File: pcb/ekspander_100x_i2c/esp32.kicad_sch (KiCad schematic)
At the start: 32 parts, among them IC1 ESP32-S3-WROOM-1U-N16R8, J25 USB4145-03-0230-C, U13 AP63203WU, U39 USBLC6-2SC6, U41 CP2102N-A02-GQFN20

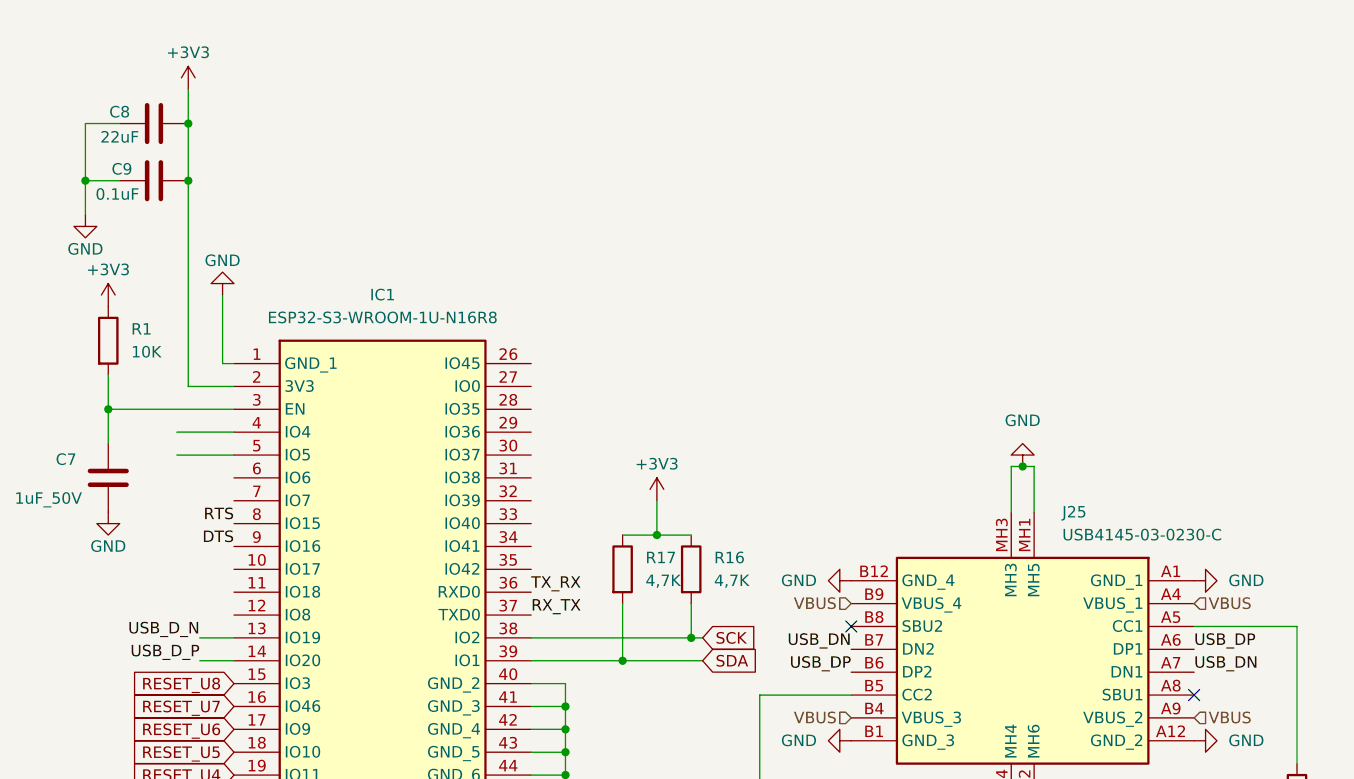
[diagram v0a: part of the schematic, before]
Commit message: Ekspander 100x - RS485
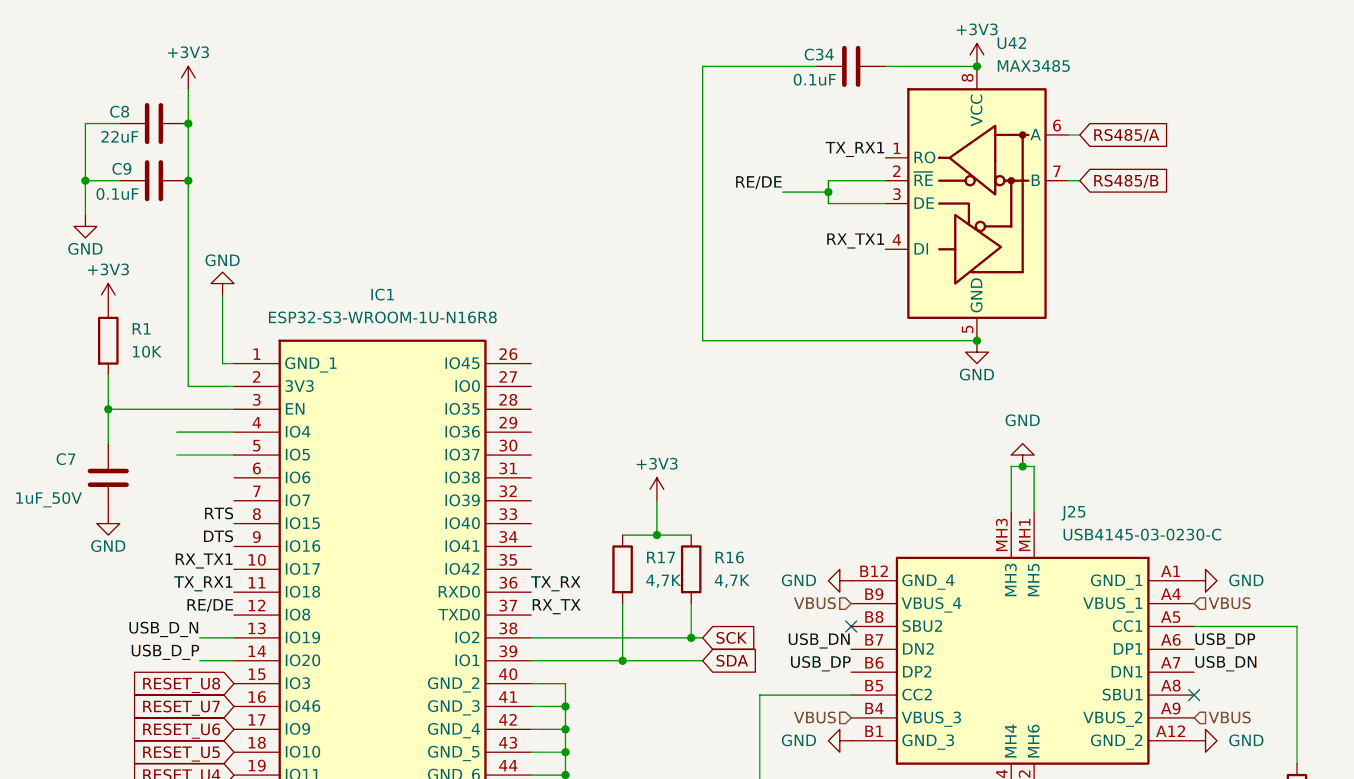
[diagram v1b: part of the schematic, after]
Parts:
- added C34: 0.1uF, Capacitor_SMD:C_0805_2012Metric_Pad1.18x1.45mm_HandSolder, symbol Device:C
- added U42: MAX3485, Package_SO:SOIC-8_3.9x4.9mm_P1.27mm, symbol Interface_UART:MAX3485
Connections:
- net +3V3: now also C34.2, U42.8 (VCC)
- net GND: now also C34.1, U42.5 (GND)
- net RX_TX1: now reaches IC1.10 (IO17)
- net RX_TX1: now also U42.4 (DI)
- net TX_RX1: now reaches IC1.11 (IO18)
- net TX_RX1: now also U42.1 (RO)
- net RE/DE: now reaches IC1.12 (IO8)
- net RE/DE: now also U42.2 (~{RE}), U42.3 (DE)
- new net RS485/A: U42.6 (A)
- new net RS485/B: U42.7 (B)
